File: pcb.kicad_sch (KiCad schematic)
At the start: 1 part, among them U1 STM32H750VBTx

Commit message: KICAD: Update project files
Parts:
- added D1: SS34, Diode_SMD:D_SOD-123F, symbol Diode:BZT52Bxx
- added J1: USB_B_Mini, symbol Connector:USB_B_Mini
- added R1: 22, symbol Device:R_US
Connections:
- new net: D1.2 (A), J1.1 (VBUS)
- no-connect marks 0 -> 1
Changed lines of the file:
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@@
     (comment 1 "First version, using swd")
+  )
+  (no_connect (at 228.6 104.14))
+  (wire (pts (xy 247.65 24.13) (xy 256.54 24.13))
+    (stroke (width 0) (type default))
+  )
+  (wire (pts (xy 256.54 24.13) (xy 256.54 29.21))
+    (stroke (width 0) (type default))
+  )
+  (symbol (lib_id "Diode:BZT52Bxx") (at 243.84 24.13 0) (unit 1)
+    (in_bom yes) (on_board yes) (dnp no) (fields_autoplaced)
+    (property "Reference" "D1" (at 243.84 17.78 0)
+      (effects (font (size 1.27 1.27)))
+    )
+    (property "Value" "SS34" (at 243.84 20.32 0)
+      (effects (font (size 1.27 1.27)))
+    )
+    (property "Footprint" "Diode_SMD:D_SOD-123F" (at 243.84 28.575 0)
+      (effects (font (size 1.27 1.27)) hide)
+    )
+    (property "Datasheet" "https://www.mouser.ca/datasheet/2/308/1/SS36FA_D-2319891.pdf" (at 243.84 24.13 0)
+      (effects (font (size 1.27 1.27)) hide)
+    )
+    (pin "1")
+    (pin "2")
+    (instances
+      (project "pcb"
+        (path "/87522a5a-c4e2-43e8-b481-132c116818d5"
+          (reference "D1") (unit 1)
+        )
+      )
+    )
+  )
+  (symbol (lib_id "Connector:USB_B_Mini") (at 264.16 34.29 0) (mirror y) (unit 1)
+    (in_bom yes) (on_board yes) (dnp no)
+    (property "Reference" "J1" (at 270.51 35.56 0)
+      (effects (font (size 1.27 1.27)) (justify right))
+    )
+    (property "Value" "USB_B_Mini" (at 270.51 33.02 0)
+      (effects (font (size 1.27 1.27)) (justify right))
+    )
+    (property "Footprint" "" (at 260.35 35.56 0)
+      (effects (font (size 1.27 1.27)) hide)
+    )
+    (property "Datasheet" "~" (at 260.35 35.56 0)
+      (effects (font (size 1.27 1.27)) hide)
+    )
+    (pin "1")
+    (pin "2")
+    (pin "3")
+    (pin "4")
+    (pin "5")
+    (pin "6")
+    (instances
+      (project "pcb"
+        (path "/87522a5a-c4e2-43e8-b481-132c116818d5"
+          (reference "J1") (unit 1)
+        )
+      )
+    )
+  )
+  (symbol (lib_id "Device:R_US") (at 246.38 36.83 90) (unit 1)
+    (in_bom yes) (on_board yes) (dnp no) (fields_autoplaced)
+    (property "Reference" "R1" (at 246.38 30.48 90)
+      (effects (font (size 1.27 1.27)))
+    )
+    (property "Value" "22" (at 246.38 33.02 90)
+      (effects (font (size 1.27 1.27)))
+    )
+    (property "Footprint" "" (at 246.634 35.814 90)
+      (effects (font (size 1.27 1.27)) hide)
+    )
+    (property "Datasheet" "~" (at 246.38 36.83 0)
+      (effects (font (size 1.27 1.27)) hide)
+    )
+    (pin "1")
+    (pin "2")
+    (instances
+      (project "pcb"
+        (path "/87522a5a-c4e2-43e8-b481-132c116818d5"
+          (reference "R1") (unit 1)
+        )
+      )
+    )
   )
   (symbol (lib_id "MCU_ST_STM32H7:STM32H750VBTx") (at 135.89 99.06 0) (unit 1)

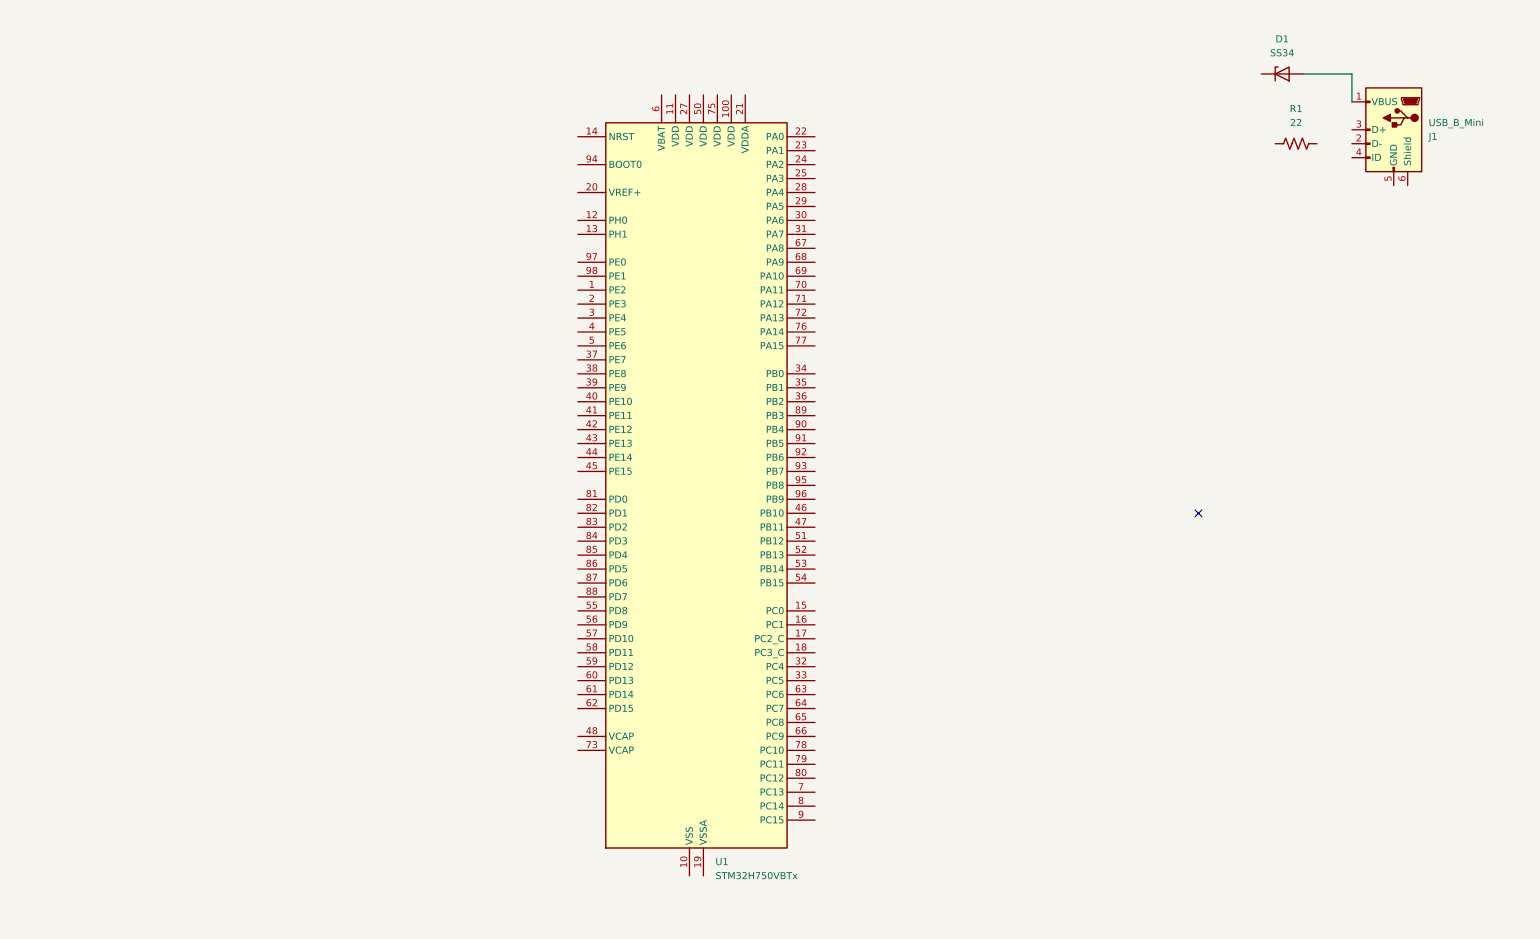
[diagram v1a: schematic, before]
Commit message: SCH: Update schematics, added everything appart from gpio pin header
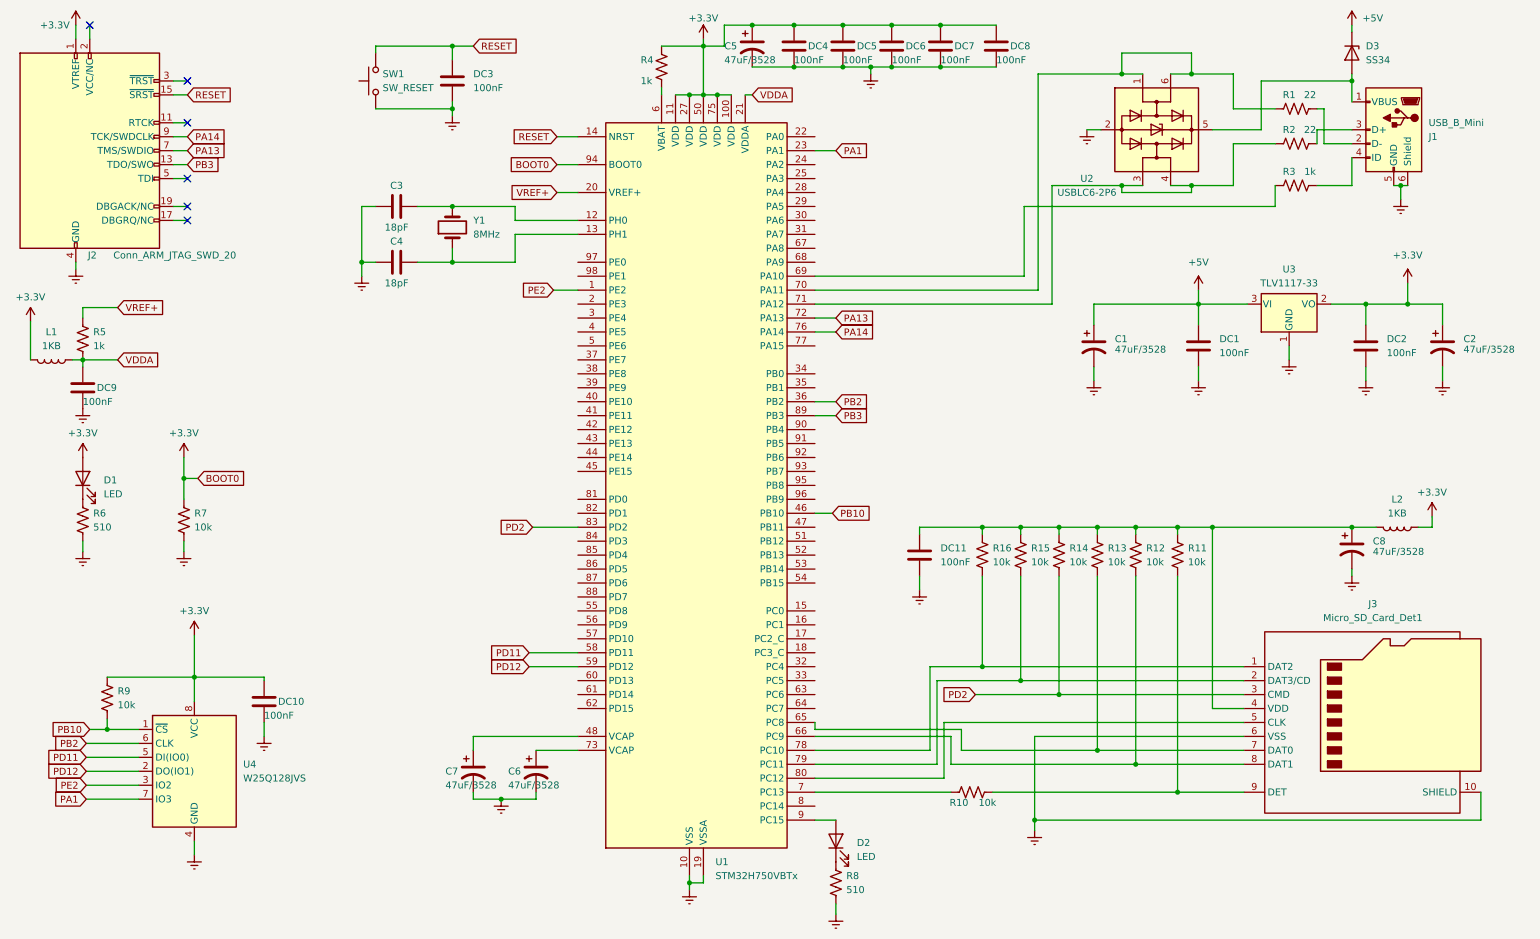
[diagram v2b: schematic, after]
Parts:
- added C1, C2, C5, C6, C7, C8: 47uF/3528, symbol Device:C_Polarized_US
- added C3, C4: 18pF, symbol Device:C
- added D1, D2: LED, symbol Device:LED
- added DC1, DC10, DC11, DC2, DC3, DC4, DC5, DC6, DC7, DC8, DC9: 100nF, symbol Device:C
- added J2: Conn_ARM_JTAG_SWD_20, symbol Connector:Conn_ARM_JTAG_SWD_20
- added J3: Micro_SD_Card_Det1, symbol Connector:Micro_SD_Card_Det1
- added L1, L2: 1KB, symbol Device:L
- added R10, R11, R12, R13, R14, R15, R16, R7, R9: 10k, symbol Device:R_US
- added R2: 22, symbol Device:R_US
- added R3, R4, R5: 1k, symbol Device:R_US
- added R6, R8: 510, symbol Device:R_US
- added SW1: SW_RESET, symbol Switch:SW_Push
- added U2: USBLC6-2P6, Package_TO_SOT_SMD:SOT-666, symbol Power_Protection:USBLC6-2P6
- added U3: TLV1117-33, symbol Regulator_Linear:TLV1117-33
- added U4: W25Q128JVS, Package_SO:SOIC-8_5.23x5.23mm_P1.27mm, symbol Memory_Flash:W25Q128JVS
- added Y1: 8MHz, symbol Device:Crystal
- renumbered D1 to D3
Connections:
- net +5V: now reaches D3.1 (K)
- net +5V: now also C1.1, DC1.1, U3.3 (VI)
- net at D3.2 (A), J1.1 (VBUS): now also U2.5 (VBUS)
- net at J1.2 (D-): now also R1.2
- net at J1.3 (D+): now also R2.2
- net at J1.4 (ID): now also R3.2
- net Earth: now reaches J1.5 (GND)
- net Earth: now also J1.6 (Shield), U1.10 (VSS), U1.19 (VSSA), U1.26 (VSS), U1.49 (VSS), U1.74 (VSS), U1.99 (VSS), C1.2, C2.2, C3.1, C4.1, C5.2, C6.2, C7.2, C8.2, DC1.2, DC10.2, DC11.2, DC2.2, DC3.2, DC4.2, DC5.2, DC6.2, DC7.2, DC8.2, DC9.2, J2.10 (GND), J2.12 (GND), J2.14 (GND), J2.16 (GND), J2.18 (GND), J2.20 (GND), J2.4 (GND), J2.6 (GND), J2.8 (GND), J3.10 (SHIELD), J3.6 (VSS), R6.2, R7.2, R8.2, SW1.1, U2.2 (GND), U3.1 (GND), U4.4 (GND)
- net at R1.1: now also U1.70 (PA11), U2.1 (I/O1), U2.6 (I/O1)
- net PE2: now reaches U1.1 (PE2)
- net PE2: now also U4.3 (IO2)
- net +3.3V: now reaches U1.100 (VDD)
- net +3.3V: now also U1.11 (VDD), U1.27 (VDD), U1.50 (VDD), U1.75 (VDD), U1.94 (BOOT0), C2.1, C5.1, D1.2 (A), DC10.1, DC2.1, DC4.1, DC5.1, DC6.1, DC7.1, DC8.1, J2.1 (VTREF), L1.2, L2.2, R4.1, R7.1, R9.1, U3.2 (VO), U4.8 (VCC)
- net at U1.12 (PH0): now also C3.2, Y1.2
- net at U1.13 (PH1): now also C4.2, Y1.1
- net RESET: now reaches U1.14 (NRST)
- net RESET: now also DC3.1, J2.15 (~{SRST}), SW1.2
- net VREF+: now reaches U1.20 (VREF+)
- net VREF+: now also R5.1
- net VDDA: now reaches U1.21 (VDDA)
- net VDDA: now also DC9.1, L1.1, R5.2
- net PA1: now reaches U1.23 (PA1)
- net PA1: now also U4.7 (IO3)
- net PB2: now reaches U1.36 (PB2)
- net PB2: now also U4.6 (CLK)
- net PB10: now reaches U1.46 (PB10)
- net PB10: now also R9.2, U4.1 (~{CS})
- net at U1.48 (VCAP): now also C7.1
- net PD11: now reaches U1.58 (PD11)
- net PD11: now also U4.5 (DI(IO0))
- net PD12: now reaches U1.59 (PD12)
- net PD12: now also U4.2 (DO(IO1))
- net at U1.6 (VBAT): now also R4.2
- net at U1.65 (PC8): now also J3.7 (DAT0), R13.2
- net at U1.66 (PC9): now also J3.8 (DAT1), R12.2
- net at U1.69 (PA10): now also R3.1
- net at U1.7 (PC13): now also R10.1
- net at U1.71 (PA12): now also R2.1, U2.3 (I/O2), U2.4 (I/O2)
- net PA13: now reaches U1.72 (PA13)
- net PA13: now also J2.7 (TMS/SWDIO)
- net at U1.73 (VCAP): now also C6.1
- net PA14: now reaches U1.76 (PA14)
- net PA14: now also J2.9 (TCK/SWDCLK)
- net at U1.78 (PC10): now also J3.1 (DAT2), R16.2
- net at U1.79 (PC11): now also J3.2 (DAT3/CD), R15.2
- net at U1.80 (PC12): now also J3.5 (CLK)
- net PD2: now reaches U1.83 (PD2)
- net PD2: now also J3.3 (CMD), R14.2
- net PB3: now reaches U1.89 (PB3)
- net PB3: now also J2.13 (TDO/SWO)
- net at U1.9 (PC15): now also D2.2 (A)
- new net: C8.1, DC11.1, J3.4 (VDD), L2.1, R11.1, R12.1, R13.1, R14.1, R15.1, R16.1
- new net: J3.9 (DET), R10.2, R11.2
- new net: D1.1 (K), R6.1
- new net: D2.1 (K), R8.1
- no-connect marks 1 -> 6
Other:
- moved on the sheet: D3, R1
